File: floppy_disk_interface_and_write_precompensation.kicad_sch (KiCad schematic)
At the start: 0 parts

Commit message: First version of the schematic completed
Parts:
- added C100: 100pF, symbol Device:C_Small
- added C66: 68pF, symbol Device:C_Small
- added C69: 47nF, symbol Device:C_Small
- added C86, C87: 1000pF, symbol Device:C_Small
- added C90, C91, C92, C93, C94, C95: 470pF, symbol Device:C_Small
- added C96, C97: 10nF, symbol Device:C_Small
- added D10, D5, D6, D7, D8, D9: 1N4148, symbol Device:D_Small_Filled
- added Q1: PN2907, symbol Device:Q_PNP_EBC
- added Q2: PN2222A, Package_TO_SOT_THT:TO-92_Inline, symbol Transistor_BJT:PN2222A
- added R11 (x5): 220R, Resistor_THT:R_Axial_DIN0207_L6.3mm_D2.5mm_P10.16mm_Horizontal, symbol Device:R_Small_US
- added R11 (x6): 330R, Resistor_THT:R_Axial_DIN0207_L6.3mm_D2.5mm_P10.16mm_Horizontal, symbol Device:R_Small_US
- added R11 (x4): 2K2, Resistor_THT:R_Axial_DIN0207_L6.3mm_D2.5mm_P10.16mm_Horizontal, symbol Device:R_Small_US
- added R11 (x2): 10K, Resistor_THT:R_Axial_DIN0207_L6.3mm_D2.5mm_P10.16mm_Horizontal, symbol Device:R_Small_US
- added R11: 270R, Resistor_THT:R_Axial_DIN0207_L6.3mm_D2.5mm_P10.16mm_Horizontal, symbol Device:R_Small_US
- added R11: 1K5, Resistor_THT:R_Axial_DIN0207_L6.3mm_D2.5mm_P10.16mm_Horizontal, symbol Device:R_Small_US
- added R11 (x3): 1K, Resistor_THT:R_Axial_DIN0207_L6.3mm_D2.5mm_P10.16mm_Horizontal, symbol Device:R_Small_US
- added R11: 3K, Resistor_THT:R_Axial_DIN0207_L6.3mm_D2.5mm_P10.16mm_Horizontal, symbol Device:R_Small_US
- added R11 (x2): 820K, Resistor_THT:R_Axial_DIN0207_L6.3mm_D2.5mm_P10.16mm_Horizontal, symbol Device:R_Small_US
- added R11 (x2): 4K7, Resistor_THT:R_Axial_DIN0207_L6.3mm_D2.5mm_P10.16mm_Horizontal, symbol Device:R_Small_US
- added R11: 51K, Resistor_THT:R_Axial_DIN0207_L6.3mm_D2.5mm_P10.16mm_Horizontal, symbol Device:R_Small_US
- added R27 (x3): 500R, symbol R_Potentiometer:R_Potentiometer_Small_US
- added TP10: READ DATA, symbol Connector:TestPoint
- added TP12: DDEN, symbol Connector:TestPoint
- added TP14: ~{FAULT_RESET}, symbol Connector:TestPoint
- added TP15: ~{FAULT_SNS}, symbol Connector:TestPoint
- added TP16: SDEN, symbol Connector:TestPoint
- added TP18: RAW, symbol Connector:TestPoint
- added TP9: WINDOW, symbol Connector:TestPoint
- added U37, U51: LS04, symbol 74xx:74LS04
- added U4 (x3): LS04, Package_DIP:DIP-14_W7.62mm_LongPads, symbol 74xx:74LS04
- added U41: DISK, symbol DIP:Conn_02x08_U41
- added U47 (x4): SYST, Package_DIP:DIP-16_W7.62mm_Socket_LongPads, symbol DIP:Conn_02x08_U47
- added U48: 74LS173, symbol LS_Logic:74LS173_U48
- added U49: uPD765, Package_DIP:DIP-40_W15.24mm, symbol FDC:uPD765
- added U50, U59: LS368, symbol LS_Logic:74LS368_U50_U59
- added U54: LS93, symbol LS_Logic:74LS93_U54
- added U55: LS109, symbol 74xx:74LS109
- added U56: LS13, symbol LS_Logic:74LS13_U56
- added U57: LS13, symbol LS_Logic:74LS13_U57
- added U58: 74LS153, symbol LS_Logic:74LS153_U58
- added U60: 7406, symbol 74xx:74LS06
- added U61: LS145, Package_DIP:DIP-16_W7.62mm, symbol LS_Logic:74LS145_U61
- added U63: LS51, symbol LS_Logic:74LS51_U63
- added U64: LS221, symbol LS_Logic:74LS221_U64
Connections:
- new net: R11.2, R27.1 (x3)
- new net: U37.2, U47.4 (Pin_4)
- new net: D10.2 (A), D9.2 (A), R11.1, U60.1
- new net: U4.1, U54.9 (Q1), U55.12 (C)
- new net: U4.2, U55.1 (~{R})
- new net: U63.10, U63.9, U64.12 (~{Q})
- new net: TP12.1, U64.5 (Q)
- new net: C92.1, C93.1, U64.6 (Cext)
- new net: C92.2, C93.2, R11.1, U64.7 (RCext)
- new net: D5.1 (K), U55.10 (Q)
- new net: D5.2 (A), D8.2 (A), R11.1
- new net: R11.1, U49.19 (~{CLK}), U51.6
- new net: U37.10, U57.10, U57.12
- new net: U47.13 (Pin_13), U57.13
- new net: U57.8, U58.15 (Eb)
- new net: U41.1 (Pin_1), U41.14 (Pin_14), U41.15 (Pin_15), U51.1
- new net: U48.7 (Cp), U51.2
- new net: U37.12, U49.1 (RST)
- new net: R11.1, U47.13 (Pin_13), U59.12 (I5)
- new net: C66.1, R11.1, R11.1, U56.2
- new net: U49.28 (US1), U61.14 (P1)
- new net: U49.29 (US0), U61.15 (P0)
- new net: U54.1 (CP1..3), U63.6
- new net: U54.12 (Q0), U63.3
- new net: R27.2, R27.3, U54.14 (CP0), U56.8, U63.5
- new net: D6.1 (K), D7.1 (K), R11.2
- new net: C96.1, C97.1, D7.2 (A), D8.1 (K), Q1.2 (B), R11.1, R11.2
- new net: U49.17 (IDX), U51.10
- new net: TP16.1, U64.13 (Q)
- new net: C90.1, C91.1, U64.14 (Cext)
- new net: C90.2, C91.2, R11.1, U64.15 (RCext)
- new net: U63.12, U63.13, U64.4 (~{Q})
- new net: Q2.1 (E), R11.2, R11.2
- new net: Q1.1 (E), Q2.2 (B), R11.1
- new net: C94.1, C95.1, R11.1, R11.1, U56.13
- new net: C86.1, C87.1, C96.2, C97.2, R11.2
- new net: U49.36 (HDL), U60.9
- new net: C86.2, C87.2, C94.2, C95.2, Q1.3 (C), R11.1, R11.1, R11.1
- new net: D9.1 (K), U49.18 (INT), U59.14 (I6)
- new net: C100.1, U58.9 (Zb)
- new net: TP14.1, U59.3 (O1a)
- new net: U58.7 (Za), U60.13
- new net: U48.12 (D2), U48.4 (Q1), U58.6 (I0a)
- new net: U48.13 (D1), U48.3 (Q0), U58.5 (I1a)
- new net: U48.5 (Q2), U58.4 (I2a)
- new net: U49.39 (~{RW}/SEEK), U51.13, U59.1 (OEa)
- new net: U49.37 (FR/STP), U50.2 (I1), U59.2 (I1)
- new net: U49.38 (LCT/DIR), U50.4 (I2), U59.4 (I2)
- new net: R11.1, R11.2, TP15.1, U59.6 (I3)
- new net: U49.33 (FLT/TR0), U50.7 (O3a), U59.7 (O3a)
- new net: U49.34 (WP/TS), U50.9 (O4a), U59.9 (O4a)
- new net: U49.25 (WE), U60.11
- new net: C66.2, U55.14 (J), U63.8
- new net: U49.27 (HD), U60.5
- new net: D6.2 (A), U55.7 (~{Q})
- new net: U47.13 (Pin_13), U60.2
- new net: U50.1 (OEa), U51.12
- new net: U49.35 (RDY), U51.8
- new net: U4.2, U55.15 (~{R})
- new net +5V: C69.1, Q2.3 (C), R11.2, R11.2, R11.2, R11.2, R11.2, R11.2, R11.2, R11.2, R11.2, R11.2, R11.2, R11.2, R11.2, R11.2, R27.2, R27.2, R27.3, R27.3, U48.16 (VCC), U49.40 (VCC), U54.5 (VCC), U58.10 (I0b), U58.11 (I1b), U58.12 (I2b), U58.13 (I3b), U58.16 (VCC), U58.3 (I3a), U61.16 (VCC)
- new net 6502_AB16: U37.1
- new net 6502_AB17: U37.11
- new net 8MHZ_CLOCK: U41.16 (Pin_16), U51.5
- new net AB_MSB: U47.4 (Pin_4)
- new net CNTA: U41.3 (Pin_3)
- new net CNTB: U41.2 (Pin_2)
- new net FDC_DATA_WINDOW: TP9.1, U49.22 (RDW), U54.8 (Q2)
- new net FDC_DRQ: U49.14 (DRQ)
- new net FDC_PS0: U49.32 (PS0), U58.14 (S0)
- new net FDC_PS1: U49.31 (PS1), U58.2 (S1)
- new net FDC_READ_DATA: TP10.1, U4.1, U49.23 (RDATA), U55.4 (C), U56.6
- new net FDC_WRT_CLK: U49.21 (WCLK)
- new net FDC_WRT_DATA: U48.14 (D0), U49.30 (WDATA)
- new net GND: C100.2, C69.2, R11.1, R11.1, R11.1, R11.1, R11.1, R11.2, R11.2, U41.8 (Pin_8), U47.4 (Pin_4), U48.1 (Oe1), U48.10 (E2), U48.15 (Mr), U48.2 (Oe2), U48.8 (GND), U48.9 (E1), U49.16 (TC), U49.20 (GND), U49.4 (~{CS}), U54.10 (GND), U54.2 (R0(1)), U54.3 (R0(2)), U58.1 (Ea), U58.8 (GND), U61.12 (P3), U61.13 (P2), U61.8 (GND)
- new net IRQ_EN: D10.1 (K)
- new net LOC_AB0: U49.5 (A0)
- new net LOC_AB15: U47.13 (Pin_13), U57.9
- new net LOC_DB0: U49.6 (DB0)
- new net LOC_DB1: U49.7 (DB1)
- new net LOC_DB2: U49.8 (DB2)
- new net LOC_DB3: U49.9 (DB3)
- new net LOC_DB4: U49.10 (DB4)
- new net LOC_DB5: U49.11 (DB5)
- new net LOC_DB6: U49.12 (DB6), U59.11 (O5b)
- new net LOC_DB7: U49.13 (DB7), U59.13 (O6b)
- new net MFM_MODE: U4.1, U49.26 (MFM), U63.11, U63.4
- new net R22: U55.11 (~{S}), U55.13 (~{K}), U55.2 (J), U55.3 (~{K}), U55.5 (~{S}), U56.1, U56.10, U56.12, U56.4, U56.5, U56.9, U64.10 (B), U64.11 (~{CLR}), U64.2 (B), U64.3 (~{CLR})
- new net ~{2_SIDE_SENSE}: R11.1, U41.9 (Pin_9), U50.10 (I4)
- new net ~{6502_IRQ}: U47.4 (Pin_4)
- new net ~{6502_RESET}: U37.13
- new net ~{DISK_RAW_RD}: R11.1, R11.1, TP18.1, U64.1 (~{A}), U64.9 (~{A})
- new net ~{DISK_WRITE_DATA}: U60.12
- new net ~{DRV_SEL_0}: U61.1 (Q0)
- new net ~{DRV_SEL_1}: U61.2 (Q1)
- new net ~{DRV_SEL_2}: U61.3 (Q2)
- new net ~{DRV_SEL_3}: U61.4 (Q3)
- new net ~{FDC_DACK}: U49.15 (~{DACK})
- new net ~{FDC_RD}: U49.2 (~{RD})
- new net ~{FDC_WRT}: U49.3 (~{WR})
- new net ~{HEAD_LOAD}: U60.8
- new net ~{HEAD_SELECT}: U60.6
- new net ~{INDEX}: R11.1, R11.2, U51.11
- new net ~{LOW_CURRENT}: U59.5 (O2a)
- new net ~{MFM_MODE}: U4.2, U63.1, U63.2
- new net ~{READY}: R11.1, U51.9
- new net ~{STATUS_READ}: U59.15 (OEb)
- new net ~{STEP_IN}: U50.5 (O2a)
- new net ~{STEP}: U50.3 (O1a)
- new net ~{TRACK_00}: R11.1, R11.2, U50.6 (I3)
- new net ~{WRITE_ENABLE}: U60.10
- new net ~{WRITE_PROT}: R11.1, R11.2, U59.10 (I4)
- no-connect marks 0 -> 12
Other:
- note added: "18 BIT ENAB"
- note added: "D DEN .5 uS"
- note added: "DATA SEPARATOR"
- note added: "DISK PRECOMP"
- note added: "DOUBLE SIDED"
- note added: "E1"
- note added: "E2"
- note added: "FLOPPY DISK INTERFACE"
- note added: "IPL OPTION"
- note added: "IRQ ENAB"
- note added: "S DEN 1.0uS"
- note added: "WRITE PRECOMPENSATION"

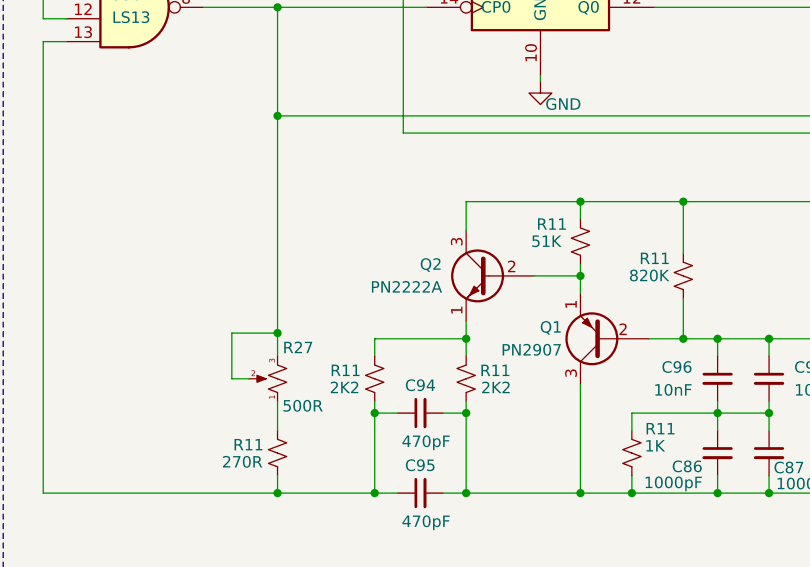
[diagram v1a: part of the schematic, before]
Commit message: Schematic corrections
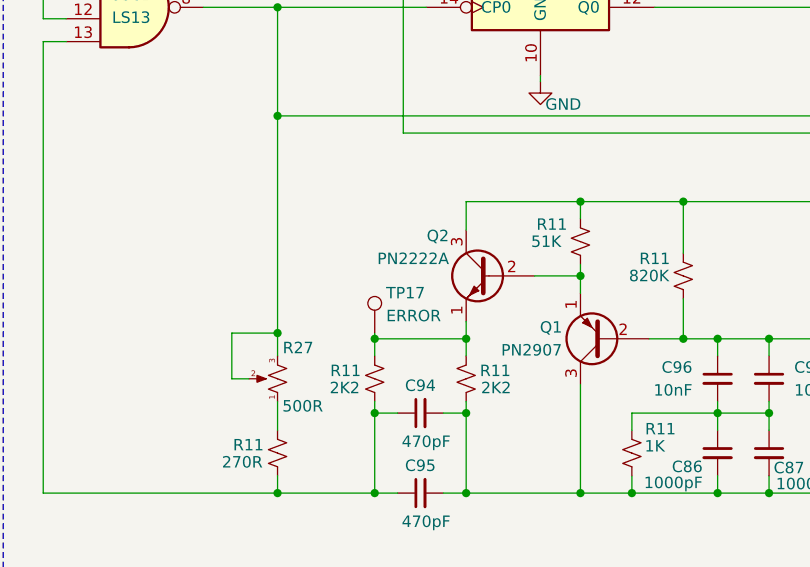
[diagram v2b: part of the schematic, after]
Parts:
- added TP17: ERROR, K_1013_Jumper:TestPoint, symbol Connector:TestPoint
- C100, C66, C69, C96, C97: footprint (none) -> K_1013_Jumper:C_Disc_D7.0mm_W2.5mm_P6.35mm
- C86, C87, C90, C91, C92, C93, C94, C95: footprint (none) -> K_1013_Jumper:C_Axial_L10.3mm_D4.7mm_P12.70mm_Horizontal
- D10, D5, D6, D7, D8, D9: footprint (none) -> K_1013_Jumper:D_DO-35_SOD27_P12.70mm_Horizontal
- Q1: footprint (none) -> K_1013_Jumper:TO-92-Custom
- Q2: footprint Package_TO_SOT_THT:TO-92_Inline -> K_1013_Jumper:TO-92-Custom
- R11: footprint Resistor_THT:R_Axial_DIN0207_L6.3mm_D2.5mm_P10.16mm_Horizontal -> K_1013_Jumper:R_Axial_DIN0309_L9.0mm_D3.2mm_P12.70mm_Horizontal
- R27: footprint (none) -> K_1013_Jumper:Potentiometer_Bourns_3339P_Vertical
- TP10, TP12, TP14, TP15, TP16, TP18, TP9: footprint (none) -> K_1013_Jumper:TestPoint
- U37, U51, U54, U56, U57, U60, U63: footprint (none) -> K_1013_Jumper:DIP-14_W7.62mm_LongPads
- U4: footprint Package_DIP:DIP-14_W7.62mm_LongPads -> K_1013_Jumper:DIP-14_W7.62mm_LongPads
- U41, U48, U50, U55, U58, U59, U64: footprint (none) -> K_1013_Jumper:DIP-16_W7.62mm_LongPads
- U47: footprint Package_DIP:DIP-16_W7.62mm_Socket_LongPads -> K_1013_Jumper:DIP-16_W7.62mm_LongPads
- U49: footprint Package_DIP:DIP-40_W15.24mm -> K_1013_Jumper:DIP-40_W15.24mm_LongPads
- U61: footprint Package_DIP:DIP-16_W7.62mm -> K_1013_Jumper:DIP-16_W7.62mm_LongPads
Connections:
- net at Q2.1 (E), R11.2, R11.2: now also TP17.1

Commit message: Update progress
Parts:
- C100, C66, C69, C96, C97: footprint K_1013_Jumper:C_Disc_D7.0mm_W2.5mm_P6.35mm -> K_1013:C_Disc_D7.0mm_W2.5mm_P6.35mm
- C86, C87, C90, C91, C92, C93, C94, C95: footprint K_1013_Jumper:C_Axial_L10.3mm_D4.7mm_P12.70mm_Horizontal -> K_1013:C_Axial_L10.3mm_D4.7mm_P12.70mm_Horizontal
- D10, D5, D6, D7, D8, D9: footprint K_1013_Jumper:D_DO-35_SOD27_P12.70mm_Horizontal -> K_1013:D_DO-35_SOD27_P12.70mm_Horizontal
- Q1, Q2: footprint K_1013_Jumper:TO-92-Custom -> K_1013:TO-92-Custom
- R16, R17, R18, R19, R23, R24, R32, R33, R34, R35, R36, R37, R38, R39, R40, R41, R43, R44, R46, R47, R50, R51, R52, R56, R57: renamed from R11; footprint K_1013_Jumper:R_Axial_DIN0309_L9.0mm_D3.2mm_P12.70mm_Horizontal -> K_1013:R_Axial_DIN0309_L9.0mm_D3.2mm_P12.70mm_Horizontal
- R25, R26, R48: renamed from R11; footprint K_1013_Jumper:R_Axial_DIN0309_L9.0mm_D3.2mm_P12.70mm_Horizontal -> K_1013:R_Axial_DIN0204_L3.6mm_D2.5mm_P12.70mm_Horizontal
- R42, R45, R49: renamed from R27; footprint K_1013_Jumper:Potentiometer_Bourns_3339P_Vertical -> K_1013:Potentiometer_Bourns_3339P_Vertical
- TP10, TP12, TP14, TP15, TP16, TP17, TP18, TP9: footprint K_1013_Jumper:TestPoint -> K_1013:TestPoint
- U37, U51, U54, U56, U57, U60, U63: footprint K_1013_Jumper:DIP-14_W7.62mm_LongPads -> K_1013:DIP-14_W7.62mm_LongPads
- U41, U47, U48, U50, U55, U58, U59, U61, U64: footprint K_1013_Jumper:DIP-16_W7.62mm_LongPads -> K_1013:DIP-16_W7.62mm_LongPads
- U49: footprint K_1013_Jumper:DIP-40_W15.24mm_LongPads -> K_1013:DIP-40_W15.24mm_LongPads
- U53: renamed from U4; footprint K_1013_Jumper:DIP-14_W7.62mm_LongPads -> K_1013:DIP-14_W7.62mm_LongPads
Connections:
- net 6502_AB16: now also U47.3 (Pin_3)
- net AB_MSB: now also U47.1 (Pin_1), U47.2 (Pin_2); no longer U47.4 (Pin_4)
- net FDC_READ_DATA: now also U53.5; no longer U53.1
- net GND: now also C86.2, C87.2, C94.2, C95.2, Q1.3 (C), R25.1, R26.1, R48.1, U47.6 (Pin_6); no longer U47.4 (Pin_4)
- net LOC_AB15: now also U47.15 (Pin_15), U57.4; no longer U47.13 (Pin_13), U57.9
- net MFM_MODE: now also U53.11; no longer U53.1
- net R22: now also U56.2; no longer U56.1
- net ~{6502_IRQ}: now also U47.8 (Pin_8); no longer U47.4 (Pin_4)
- net ~{MFM_MODE}: now also U53.10; no longer U53.2
- net at U37.2: now also U47.5 (Pin_5); no longer U47.4 (Pin_4)
- net at U54.9 (Q1), U55.12 (C): now also U53.9; no longer U53.1
- net at U55.1 (~{R}): now also U53.8; no longer U53.2
- net at U58.15 (Eb): now also U57.6; no longer U57.8
- net at R18.1, U59.12 (I5): now also U47.11 (Pin_11); no longer U47.13 (Pin_13)
- net at C66.1, R16.1, R17.1: now also U56.1; no longer U56.2
- net at C100.1, U58.9 (Zb): now also U47.16 (Pin_16)
- net at U60.2: now also U47.9 (Pin_9); no longer U47.13 (Pin_13)
- net at U55.15 (~{R}): now also U53.6; no longer U53.2
- new net: U37.10, U57.1, U57.2
- new net: U47.12 (Pin_12), U47.14 (Pin_14), U57.5

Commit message: Routing of the bottom layer completed
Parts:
- U37: footprint K_1013:DIP-14_W7.62mm_LongPads -> K_1013:DIP-14_W7.62mm_LongPads_U37
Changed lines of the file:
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@@
       (effects (font (size 1.27 1.27)))
     )
-    (property "Footprint" "K_1013:DIP-14_W7.62mm_LongPads" (at 218.44 78.74 0)
+    (property "Footprint" "K_1013:DIP-14_W7.62mm_LongPads_U37" (at 218.44 78.74 0)
       (effects (font (size 1.27 1.27)) hide)
     )
@@
       (effects (font (size 1.27 1.27)))
     )
-    (property "Footprint" "K_1013:DIP-14_W7.62mm_LongPads" (at 61.595 102.87 0)
+    (property "Footprint" "K_1013:DIP-14_W7.62mm_LongPads_U37" (at 61.595 102.87 0)
       (effects (font (size 1.27 1.27)) hide)
     )
@@
       (effects (font (size 1.27 1.27)))
     )
-    (property "Footprint" "K_1013:DIP-14_W7.62mm_LongPads" (at 218.44 69.215 0)
-      (effects (font (size 1.27 1.27)) hide)
-    )
+    (property "Footprint" "K_1013:DIP-14_W7.62mm_LongPads_U37" (at 218.44 69.215 0)
+      (effects (font (size 1.27 1.27)) hide)
+    )

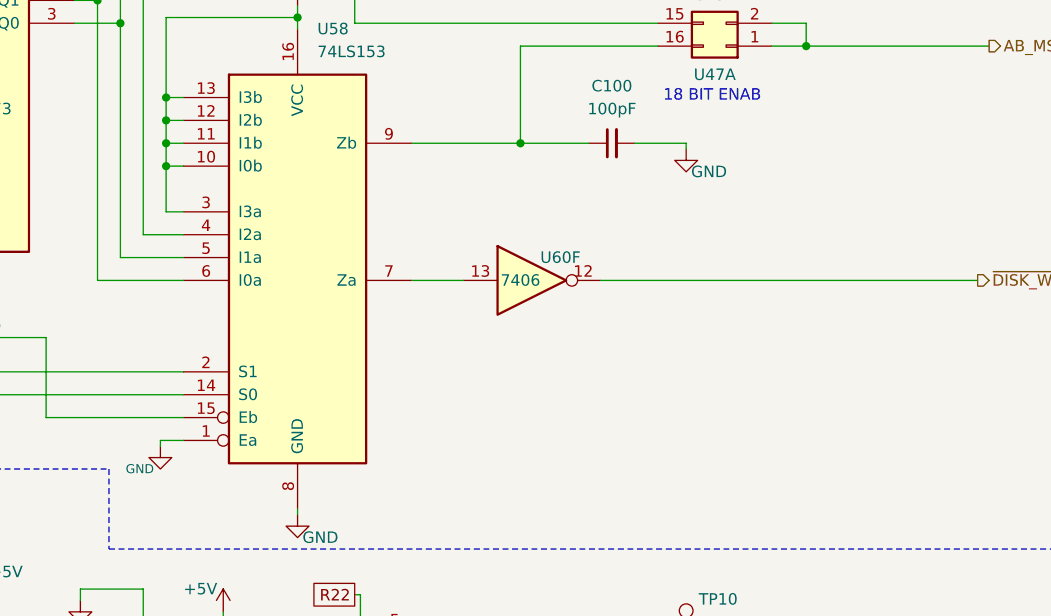
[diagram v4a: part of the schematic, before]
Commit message: Completed first version of board routing
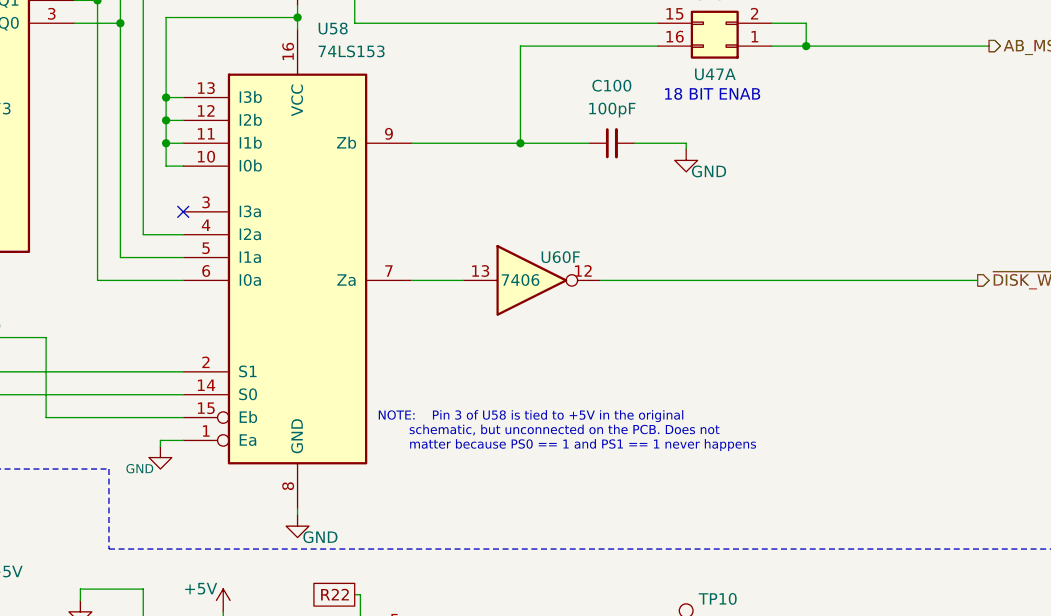
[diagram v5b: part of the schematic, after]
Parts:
- R16, R17, R47: footprint K_1013:R_Axial_DIN0309_L9.0mm_D3.2mm_P12.70mm_Horizontal -> K_1013:R_Axial_DIN0204_L3.6mm_D2.5mm_P12.70mm_Horizontal_2K2
- R18, R57: footprint K_1013:R_Axial_DIN0309_L9.0mm_D3.2mm_P12.70mm_Horizontal -> K_1013:R_Axial_DIN0204_L3.6mm_D2.5mm_P12.70mm_Horizontal_10K
- R19, R56: footprint K_1013:R_Axial_DIN0309_L9.0mm_D3.2mm_P12.70mm_Horizontal -> K_1013:R_Axial_DIN0204_L3.6mm_D2.5mm_P12.70mm_Horizontal_1K
- R23, R24: footprint K_1013:R_Axial_DIN0309_L9.0mm_D3.2mm_P12.70mm_Horizontal -> K_1013:R_Axial_DIN0204_L3.6mm_D2.5mm_P12.70mm_Horizontal_4K7
- R25: footprint K_1013:R_Axial_DIN0204_L3.6mm_D2.5mm_P12.70mm_Horizontal -> K_1013:R_Axial_DIN0204_L3.6mm_D2.5mm_P12.70mm_Horizontal_820K
- R26: footprint K_1013:R_Axial_DIN0204_L3.6mm_D2.5mm_P12.70mm_Horizontal -> K_1013:R_Axial_DIN0204_L3.6mm_D2.5mm_P12.70mm_Horizontal_1K
- R32, R34, R36, R38, R41: footprint K_1013:R_Axial_DIN0309_L9.0mm_D3.2mm_P12.70mm_Horizontal -> K_1013:R_Axial_DIN0204_L3.6mm_D2.5mm_P12.70mm_Horizontal_220R
- R33, R35, R37, R39, R40, R52: footprint K_1013:R_Axial_DIN0309_L9.0mm_D3.2mm_P12.70mm_Horizontal -> K_1013:R_Axial_DIN0204_L3.6mm_D2.5mm_P12.70mm_Horizontal_330R
- R43: footprint K_1013:R_Axial_DIN0309_L9.0mm_D3.2mm_P12.70mm_Horizontal -> K_1013:R_Axial_DIN0204_L3.6mm_D2.5mm_P12.70mm_Horizontal_3K
- R44: footprint K_1013:R_Axial_DIN0309_L9.0mm_D3.2mm_P12.70mm_Horizontal -> K_1013:R_Axial_DIN0204_L3.6mm_D2.5mm_P12.70mm_Horizontal_1K5
- R46: footprint K_1013:R_Axial_DIN0309_L9.0mm_D3.2mm_P12.70mm_Horizontal -> K_1013:R_Axial_DIN0204_L3.6mm_D2.5mm_P12.70mm_Horizontal_270R
- R48: footprint K_1013:R_Axial_DIN0204_L3.6mm_D2.5mm_P12.70mm_Horizontal -> K_1013:R_Axial_DIN0204_L3.6mm_D2.5mm_P12.70mm_Horizontal_2K2
- R50: footprint K_1013:R_Axial_DIN0309_L9.0mm_D3.2mm_P12.70mm_Horizontal -> K_1013:R_Axial_DIN0204_L3.6mm_D2.5mm_P12.70mm_Horizontal_51K
- R51: footprint K_1013:R_Axial_DIN0309_L9.0mm_D3.2mm_P12.70mm_Horizontal -> K_1013:R_Axial_DIN0204_L3.6mm_D2.5mm_P12.70mm_Horizontal_820K
- U41, U47: footprint K_1013:DIP-16_W7.62mm_LongPads -> K_1013:DIP-16_W7.62mm_LongPads_SW
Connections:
- net +5V: no longer U58.3 (I3a)
- no-connect marks 12 -> 13
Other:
- note added: "NOTE: Pin 3 of U58 is tied to +5V in the original schematic, but unconnected on the PCB. Does not matter because PS0 == 1 and PS1 == 1 never happens"
